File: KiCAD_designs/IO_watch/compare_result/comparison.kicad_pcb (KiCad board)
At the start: 2 copper layers, 38.8 x 34.7 mm, 39 parts, among them U1 ATMEGA328P-AU, U2 DS3231S

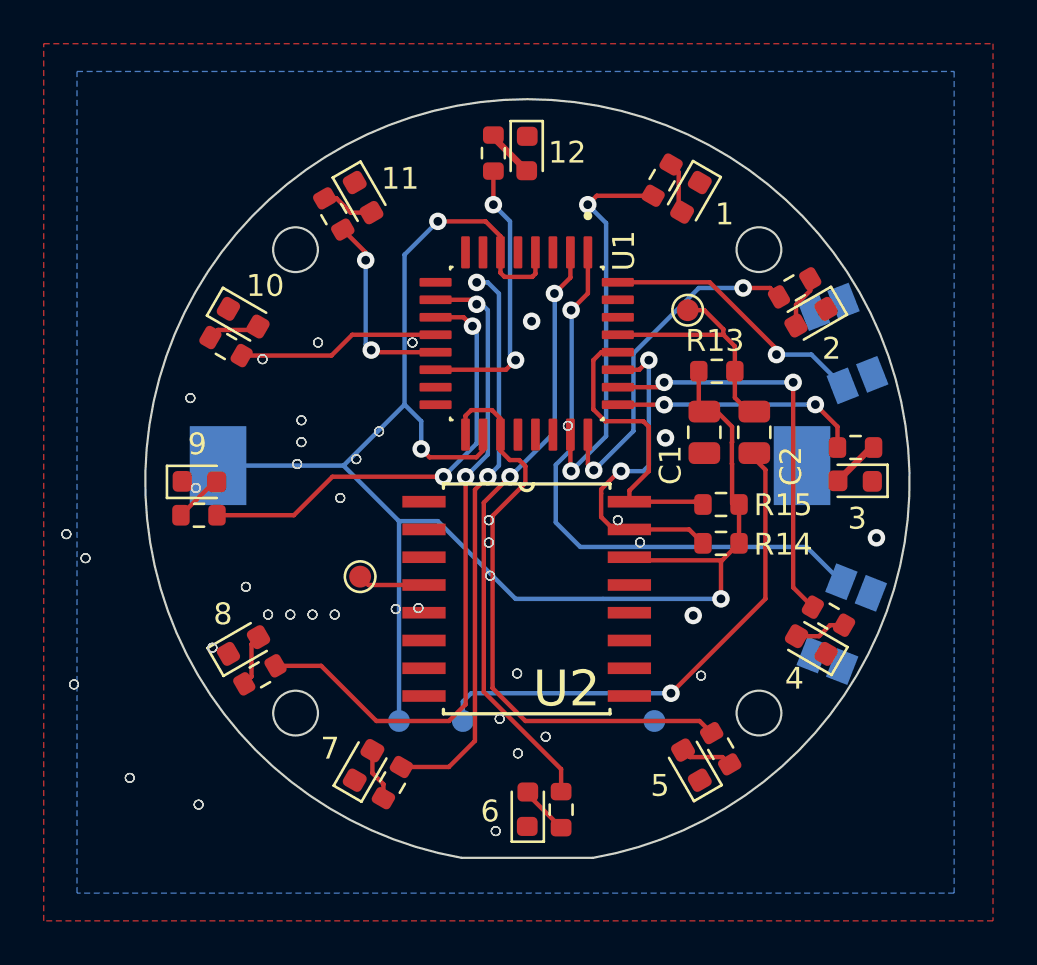
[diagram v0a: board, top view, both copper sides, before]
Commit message: changed cat ball via size
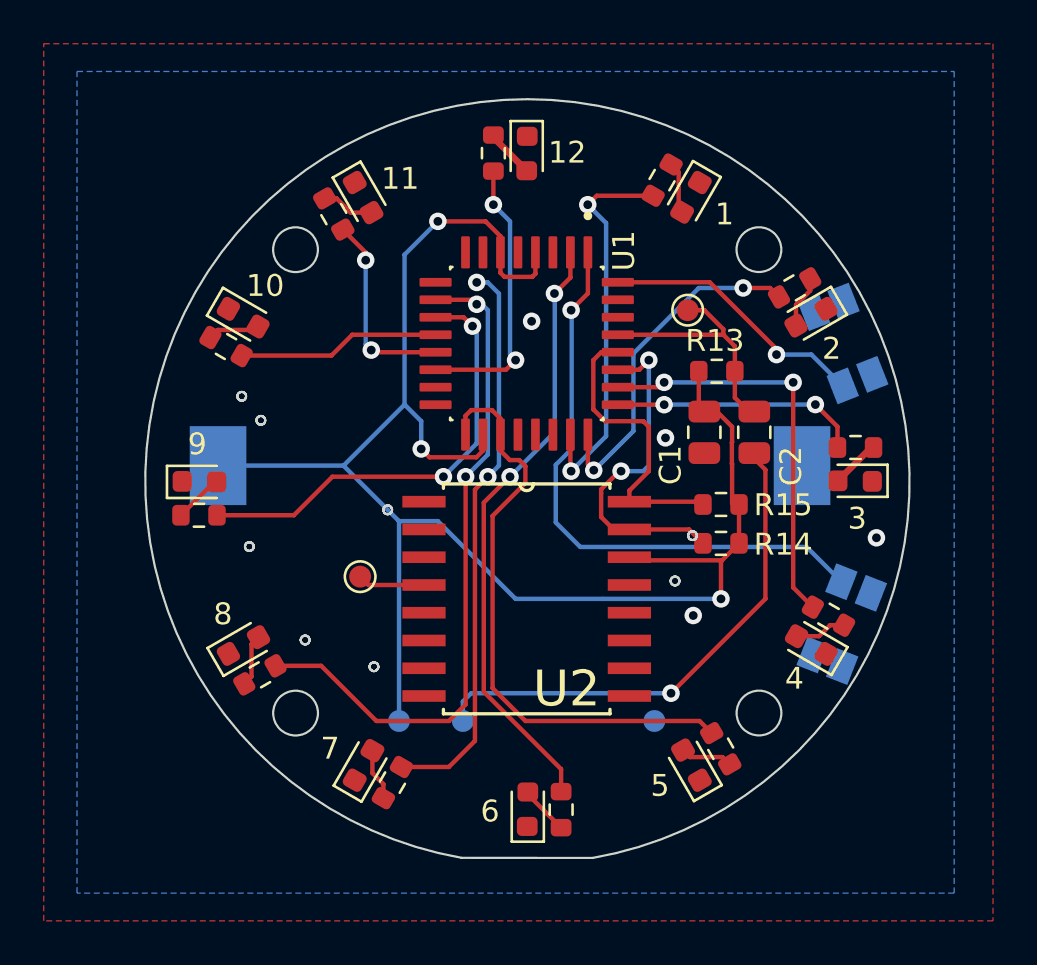
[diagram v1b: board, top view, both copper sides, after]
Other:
- board size 38.8 x 34.7 mm -> 35 x 34.7 mm
